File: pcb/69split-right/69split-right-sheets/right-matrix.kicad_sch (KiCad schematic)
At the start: 78 parts, among them SW1 SW_Push, SW10 SW_Push, SW11 SW_Push, SW12 SW_Push, SW13 SW_Push, SW14 SW_Push, SW15 SW_Push, SW16 SW_Push, SW17 SW_Push, SW18 SW_Push, SW19 SW_Push, SW2 SW_Push, SW20 SW_Push, SW21 SW_Push, SW22 SW_Push, SW23 SW_Push, SW24 SW_Push, SW25 SW_Push, SW26 SW_Push, SW27 SW_Push, SW28 SW_Push, SW29 SW_Push, SW3 SW_Push, SW30 SW_Push, SW31 SW_Push, SW32 SW_Push, SW33 SW_Push, SW34 SW_Push, SW35 SW_Push, SW36 SW_Push, SW37 SW_Push, SW38 SW_Push, SW39 SW_Push, SW4 SW_Push, SW5 SW_Push, SW6 SW_Push, SW7 SW_Push, SW8 SW_Push, SW9 SW_Push

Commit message: More final touches fml.
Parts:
- SW31: Key ↑ -> Up
- SW37: Key ← -> Left
- SW38: Key ↓ -> Down
- SW39: Key → -> Right
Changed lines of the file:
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@@
 			)
 		)
-		(property "Key" "←"
+		(property "Key" "Left"
 			(at 195.58 123.19 0)
 			(effects
@@
 			)
 		)
-		(property "Key" "↑"
+		(property "Key" "Up"
 			(at 215.9 110.49 0)
 			(effects
@@
 			)
 		)
-		(property "Key" "→"
+		(property "Key" "Right"
 			(at 234.95 123.19 0)
 			(effects
@@
 			)
 		)
-		(property "Key" "↓"
+		(property "Key" "Down"
 			(at 215.9 123.19 0)
 			(effects

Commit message: Ordered the PCBs and parts!
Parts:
- D1, D10, D11, D12, D13, D14, D15, D16, D17, D18, D19, D2, D20, D21, D22, D23, D24, D25, D26, D27, D28, D29, D3, D30, D31, D32, D33, D34, D35, D36, D37, D38, D39, D4, D5, D6, D7, D8, D9: MPN 1N4454 -> 1N4148
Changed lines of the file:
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@@
 			)
 		)
-		(property "MPN" "1N4454"
+		(property "MPN" "1N4148"
 			(at 200.66 121.92 90)
 			(effects
@@
 			)
 		)
-		(property "MPN" "1N4454"
+		(property "MPN" "1N4148"
 			(at 200.66 83.82 90)
 			(effects
@@
 			)
 		)
-		(property "MPN" "1N4454"
+		(property "MPN" "1N4148"
 			(at 240.03 109.22 90)
 			(effects
@@
 			)
 		)
-		(property "MPN" "1N4454"
+		(property "MPN" "1N4148"
 			(at 139.7 96.52 90)
 			(effects
@@
 			)
 		)
-		(property "MPN" "1N4454"
+		(property "MPN" "1N4148"
 			(at 220.98 71.12 90)
 			(effects
@@
 			)
 		)
-		(property "MPN" "1N4454"
+		(property "MPN" "1N4148"
 			(at 161.29 121.92 90)
 			(effects
@@
 			)
 		)
-		(property "MPN" "1N4454"
+		(property "MPN" "1N4148"
 			(at 200.66 96.52 90)
 			(effects
@@
 			)
 		)
-		(property "MPN" "1N4454"
+		(property "MPN" "1N4148"
 			(at 180.34 83.82 90)
 			(effects
@@
 			)
 		)
-		(property "MPN" "1N4454"
+		(property "MPN" "1N4148"
 			(at 100.33 83.82 90)
 			(effects
@@
 			)
 		)
-		(property "MPN" "1N4454"
+		(property "MPN" "1N4148"
 			(at 100.33 96.52 90)
 			(effects
@@
 			)
 		)
-		(property "MPN" "1N4454"
+		(property "MPN" "1N4148"
 			(at 119.38 71.12 90)
 			(effects
@@
 			)
 		)
-		(property "MPN" "1N4454"
+		(property "MPN" "1N4148"
 			(at 161.29 109.22 90)
 			(effects
@@
 			)
 		)
-		(property "MPN" "1N4454"
+		(property "MPN" "1N4148"
 			(at 220.98 109.22 90)
 			(effects
@@
 			)
 		)
-		(property "MPN" "1N4454"
+		(property "MPN" "1N4148"
 			(at 100.33 71.12 90)
 			(effects
@@
 			)
 		)
-		(property "MPN" "1N4454"
+		(property "MPN" "1N4148"
 			(at 139.7 109.22 90)
 			(effects
@@
 			)
 		)
-		(property "MPN" "1N4454"
+		(property "MPN" "1N4148"
 			(at 220.98 83.82 90)
 			(effects
@@
 			)
 		)
-		(property "MPN" "1N4454"
+		(property "MPN" "1N4148"
 			(at 100.33 121.92 90)
 			(effects
@@
 			)
 		)
-		(property "MPN" "1N4454"
+		(property "MPN" "1N4148"
 			(at 200.66 109.22 90)
 			(effects
@@
 			)
 		)
-		(property "MPN" "1N4454"
+		(property "MPN" "1N4148"
 			(at 220.98 96.52 90)
 			(effects
@@
 			)
 		)
-		(property "MPN" "1N4454"
+		(property "MPN" "1N4148"
 			(at 180.34 71.12 90)
 			(effects
@@
 			)
 		)
-		(property "MPN" "1N4454"
+		(property "MPN" "1N4148"
 			(at 240.03 71.12 90)
 			(effects
@@
 			)
 		)
-		(property "MPN" "1N4454"
+		(property "MPN" "1N4148"
 			(at 220.98 121.92 90)
 			(effects
@@
 			)
 		)
-		(property "MPN" "1N4454"
+		(property "MPN" "1N4148"
 			(at 240.03 96.52 90)
 			(effects
@@
 			)
 		)
-		(property "MPN" "1N4454"
+		(property "MPN" "1N4148"
 			(at 161.29 96.52 90)
 			(effects
@@
 			)
 		)
-		(property "MPN" "1N4454"
+		(property "MPN" "1N4148"
 			(at 139.7 83.82 90)
 			(effects
@@
 			)
 		)
-		(property "MPN" "1N4454"
+		(property "MPN" "1N4148"
 			(at 119.38 96.52 90)
 			(effects
@@
 			)
 		)
-		(property "MPN" "1N4454"
+		(property "MPN" "1N4148"
 			(at 180.34 96.52 90)
 			(effects
@@
 			)
 		)
-		(property "MPN" "1N4454"
+		(property "MPN" "1N4148"
 			(at 119.38 83.82 90)
 			(effects
@@
 			)
 		)
-		(property "MPN" "1N4454"
+		(property "MPN" "1N4148"
 			(at 180.34 121.92 90)
 			(effects
@@
 			)
 		)
-		(property "MPN" "1N4454"
+		(property "MPN" "1N4148"
 			(at 139.7 71.12 90)
 			(effects
@@
 			)
 		)
-		(property "MPN" "1N4454"
+		(property "MPN" "1N4148"
 			(at 200.66 71.12 90)
 			(effects
@@
 			)
 		)
-		(property "MPN" "1N4454"
+		(property "MPN" "1N4148"
 			(at 139.7 121.92 90)
 			(effects
@@
 			)
 		)
-		(property "MPN" "1N4454"
+		(property "MPN" "1N4148"
 			(at 180.34 109.22 90)
 			(effects
@@
 			)
 		)
-		(property "MPN" "1N4454"
+		(property "MPN" "1N4148"
 			(at 161.29 83.82 90)
 			(effects
@@
 			)
 		)
-		(property "MPN" "1N4454"
+		(property "MPN" "1N4148"
 			(at 119.38 109.22 90)
 			(effects
@@
 			)
 		)
-		(property "MPN" "1N4454"
+		(property "MPN" "1N4148"
 			(at 240.03 83.82 90)
 			(effects
@@
 			)
 		)
-		(property "MPN" "1N4454"
+		(property "MPN" "1N4148"
 			(at 161.29 71.12 90)
 			(effects
@@
 			)
 		)
-		(property "MPN" "1N4454"
+		(property "MPN" "1N4148"
 			(at 240.03 121.92 90)
 			(effects
@@
 			)
 		)
-		(property "MPN" "1N4454"
+		(property "MPN" "1N4148"
 			(at 100.33 109.22 90)
 			(effects

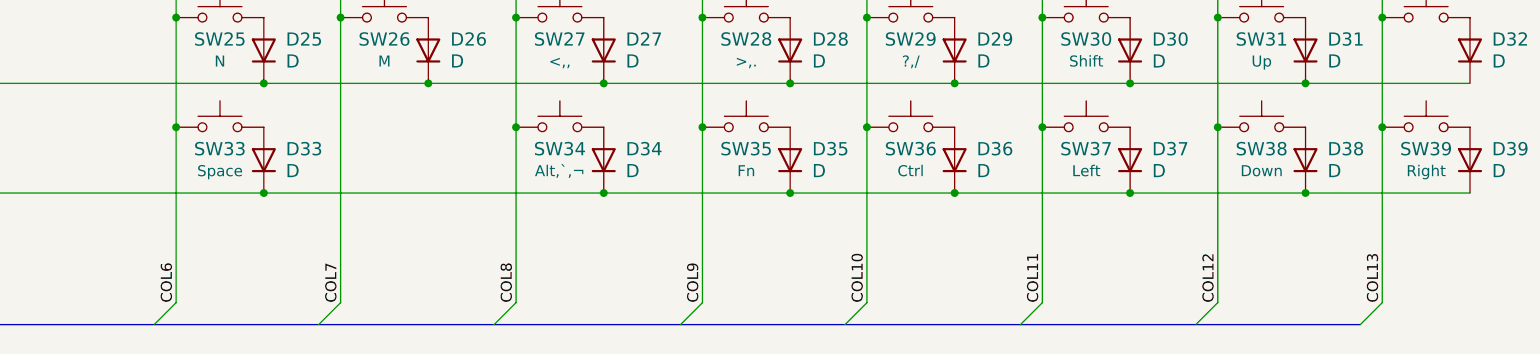
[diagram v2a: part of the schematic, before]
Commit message: Fix column number labels
Before it started from COL6 but it should start from COL7 because COL6
is on the left PCB.
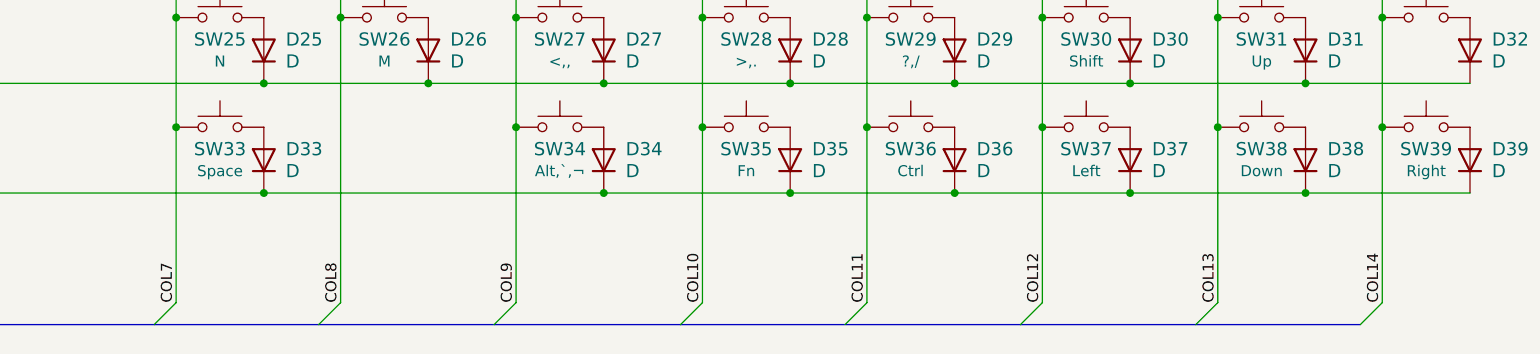
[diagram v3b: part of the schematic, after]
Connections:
- net COL6 is gone; now on net COL7: SW1.1, SW17.1, SW25.1, SW33.1, SW9.1
- net COL10: now also SW12.1, SW20.1, SW28.1, SW35.1, SW4.1; no longer SW13.1, SW21.1, SW29.1, SW36.1, SW5.1
- net COL11: now also SW13.1, SW21.1, SW29.1, SW36.1, SW5.1; no longer SW14.1, SW22.1, SW30.1, SW37.1, SW6.1
- net COL12: now also SW14.1, SW22.1, SW30.1, SW37.1, SW6.1; no longer SW15.1, SW23.1, SW31.1, SW38.1, SW7.1
- net COL13: now also SW15.1, SW23.1, SW31.1, SW38.1, SW7.1; no longer SW16.1, SW24.1, SW32.1, SW39.1, SW8.1
- net COL7: no longer SW10.1, SW18.1, SW2.1, SW26.1
- net COL8: now also SW10.1, SW18.1, SW2.1, SW26.1; no longer SW11.1, SW19.1, SW27.1, SW3.1, SW34.1
- net COL9: now also SW11.1, SW19.1, SW27.1, SW3.1, SW34.1; no longer SW12.1, SW20.1, SW28.1, SW35.1, SW4.1
- new net COL14: SW16.1, SW24.1, SW32.1, SW39.1, SW8.1
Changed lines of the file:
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@@
 		)
 	)
-	(label "COL11"
+	(label "COL12"
 		(at 190.5 138.43 90)
 		(effects
@@
 		)
 	)
-	(label "COL9"
+	(label "COL10"
 		(at 151.13 138.43 90)
 		(effects
@@
 		)
 	)
-	(label "COL10"
+	(label "COL11"
 		(at 170.18 138.43 90)
 		(effects
@@
 		)
 	)
-	(label "COL12"
+	(label "COL13"
 		(at 210.82 138.43 90)
 		(effects
@@
 		)
 	)
-	(label "COL8"
+	(label "COL9"
 		(at 129.54 138.43 90)
 		(effects
@@
 		)
 	)
-	(label "COL6"
+	(label "COL7"
 		(at 90.17 138.43 90)
 		(effects
@@
 		)
 	)
-	(label "COL13"
+	(label "COL14"
 		(at 229.87 138.43 90)
 		(effects
@@
 		)
 	)
-	(label "COL7"
+	(label "COL8"
 		(at 109.22 138.43 90)
 		(effects

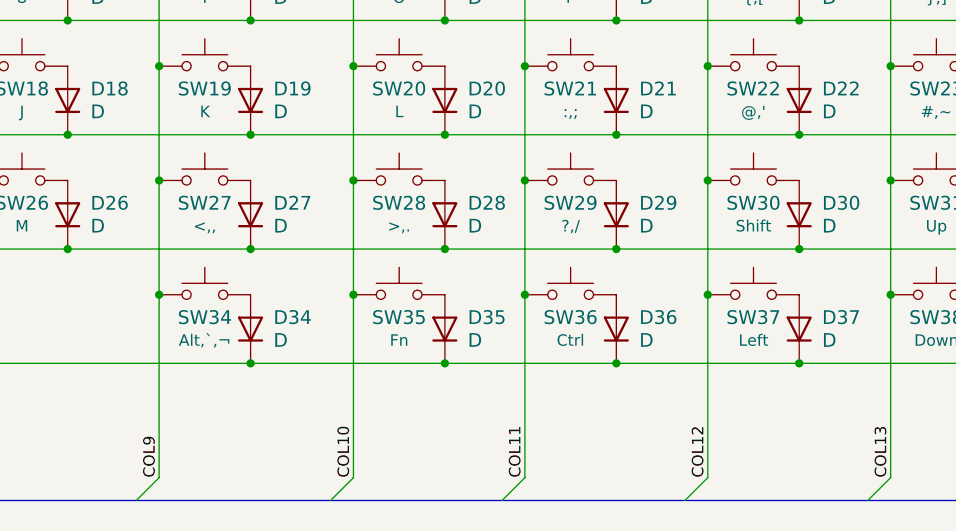
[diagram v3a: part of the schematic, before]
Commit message: Update key names
Change Win to GUI and specify L/R Alt, L/R Shift, and L/R Ctrl
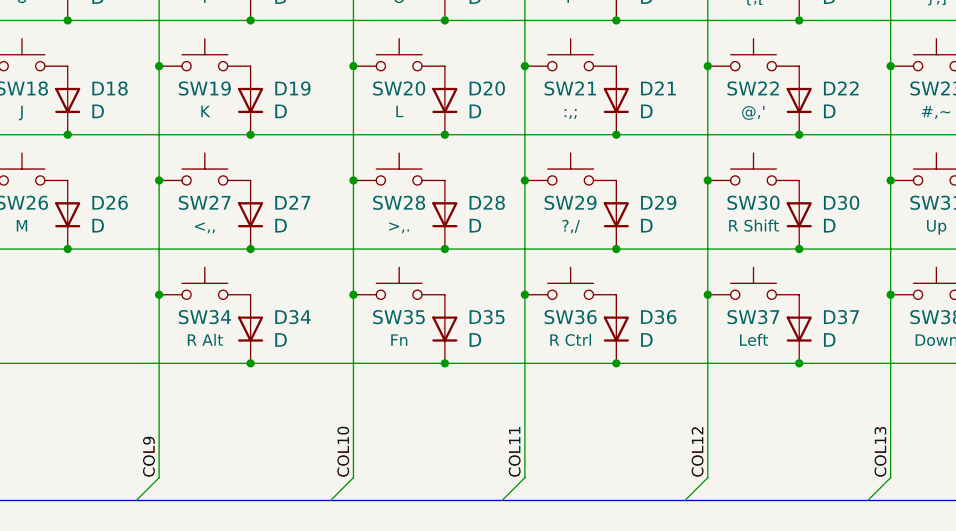
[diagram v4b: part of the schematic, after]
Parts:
- SW30: Key Shift -> R Shift
- SW34: Key Alt,`,¬ -> R Alt
- SW36: Key Ctrl -> R Ctrl
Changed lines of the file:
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@@
 			)
 		)
-		(property "Key" "Shift"
+		(property "Key" "R Shift"
 			(at 195.58 110.49 0)
 			(effects
@@
 			)
 		)
-		(property "Key" "Alt,`,¬"
+		(property "Key" "R Alt"
 			(at 134.62 123.19 0)
 			(effects
@@
 			)
 		)
-		(property "Key" "Ctrl"
+		(property "Key" "R Ctrl"
 			(at 175.26 123.19 0)
 			(effects
